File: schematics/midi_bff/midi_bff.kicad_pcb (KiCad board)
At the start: 2 copper layers, 61 x 45.7 mm, 17 parts, among them CN1 DIN-504, CN2 DIN-504, J1 PJ-320A-4P DIP, J2 PJ-320A-4P DIP, U3 H11L1

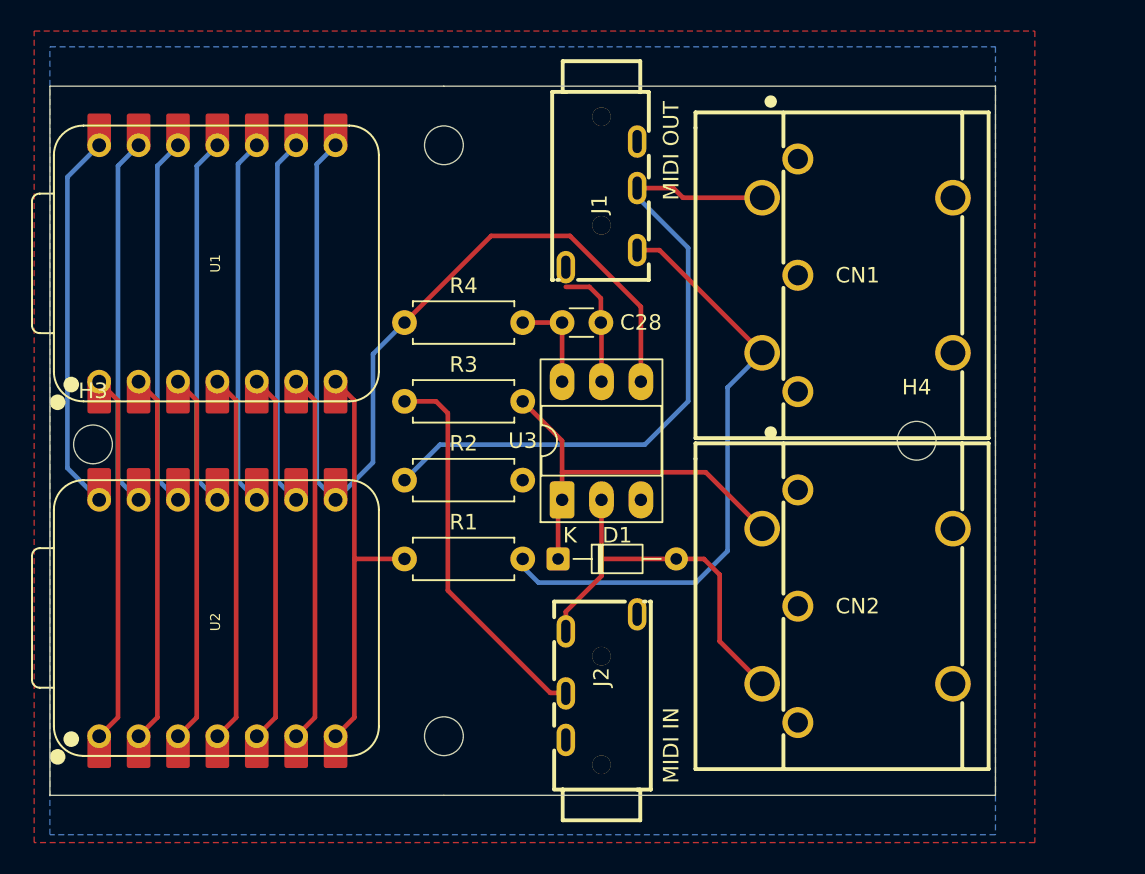
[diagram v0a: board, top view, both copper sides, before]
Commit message: sent to production
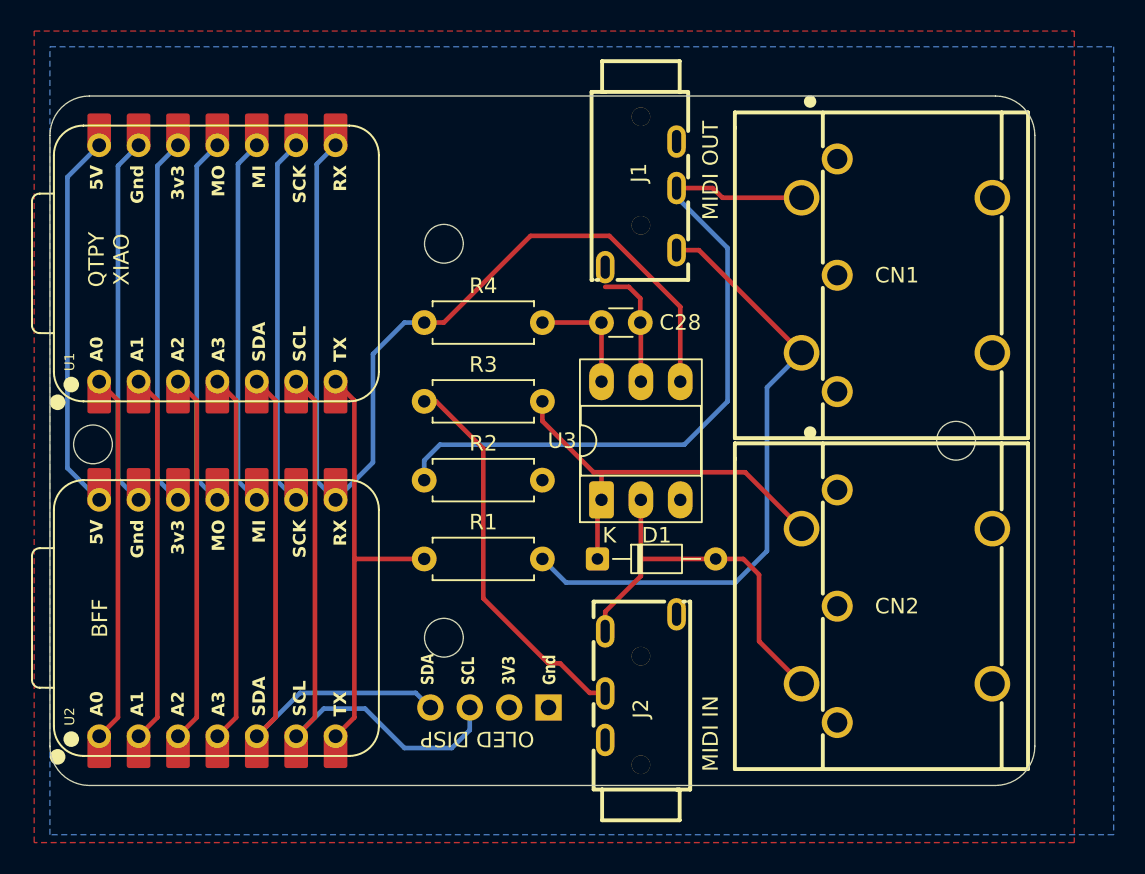
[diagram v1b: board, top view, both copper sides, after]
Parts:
- added J3: OLED-128x32, kleeb-display:OLED-128x32, F.Cu at (98.5, 95.0)
- moved H1 6.35 mm to (101.6, 63.5)
- moved H2 6.35 mm to (101.6, 88.9)
- moved C28 2.54 mm to (111.8, 68.6)
- moved D1 2.54 mm to (111.5, 83.8)
- moved U3 2.54 mm to (111.8, 80.0)
- moved CN1 2.54 mm to (130.8, 65.5)
- moved CN2 2.54 mm to (130.8, 86.9)
- moved H4 2.54 mm to (134.6, 76.2)
- moved J1 2.54 mm to (114.3, 61.0)
- moved J2 2.54 mm to (114.3, 91.4)
- moved R1 1.27 mm to (100.3, 83.8)
- moved R2 1.27 mm to (100.3, 78.7)
- moved R3 1.27 mm to (100.3, 73.7)
- moved R4 1.27 mm to (100.3, 68.6)
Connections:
- net /Net-(U6-SCL) renamed /SCL
- net /Net-(U6-SDA) renamed /SDA
- CN1 pad 2: /unconnected-(CN2-Pad2) -> unconnected-(CN1-Pad2)
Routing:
- net /SCL: track 23.9 -> 38.8 mm
- net /SDA: track 23.9 -> 36.6 mm
- net /MIDI_IN: track 61.4 -> 64.0 mm
- net Net-(CN1-Pad4): track 43.3 -> 45.3 mm
- net /MIDI_OUT: track 27.1 -> 28.4 mm
- net +3V3: track 30.3 -> 31.6 mm
- net Net-(D1-K): track 25.7 -> 26.5 mm
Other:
- board size 61 x 45.7 mm -> 63.5 x 44.4 mm
- board text added: "5V Gnd 3v3 MO MI SCK RX"
- board text added: "A0 A1 A2 A3 SDA SCL TX"
- board text added: "BFF"
- board text added: "MIDI IN TRS-A"
- board text added: "MIDI OUT TRS-A"
- board text added: "OLED DISP"
- board text added: "QTPY / XIAO MIDI BFF"
- board text added: "QTPY XIAO"
- board text added: "SDA SCL 3V3 Gnd"
- board text added: "github.com/todbot/qtpy_midibff 2026 May 8 - @todbot"
